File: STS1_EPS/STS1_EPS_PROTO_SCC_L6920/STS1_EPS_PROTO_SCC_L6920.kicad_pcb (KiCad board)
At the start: 2 copper layers, 15 parts, among them J1 Screw_Terminal_01x02, J2 Screw_Terminal_01x02, Q1 2N7000

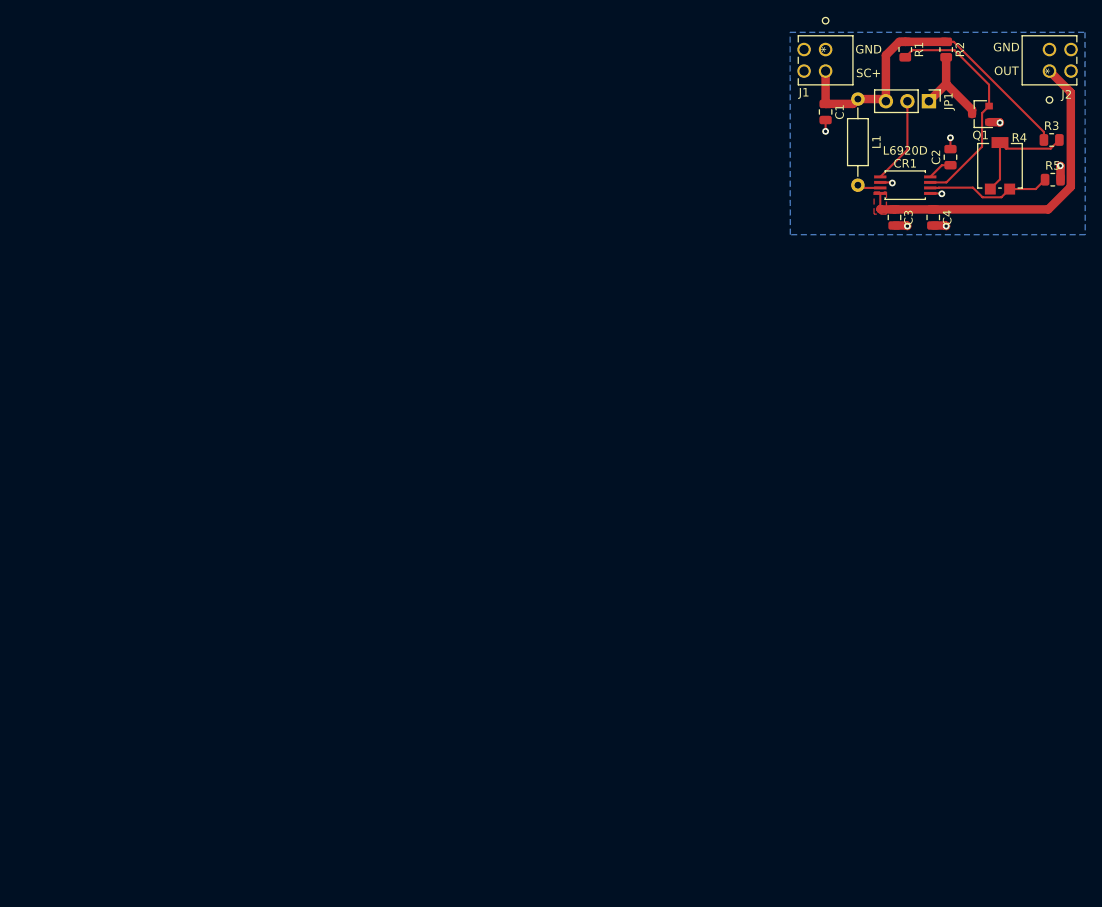
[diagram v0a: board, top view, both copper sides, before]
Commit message: - STS1_EPS_PROTO_SCC_L6920 now uses the STS1 PCB template and is again ready for review. - WOrked on STS1_EPS_PROTO_BCC_LTC4020.
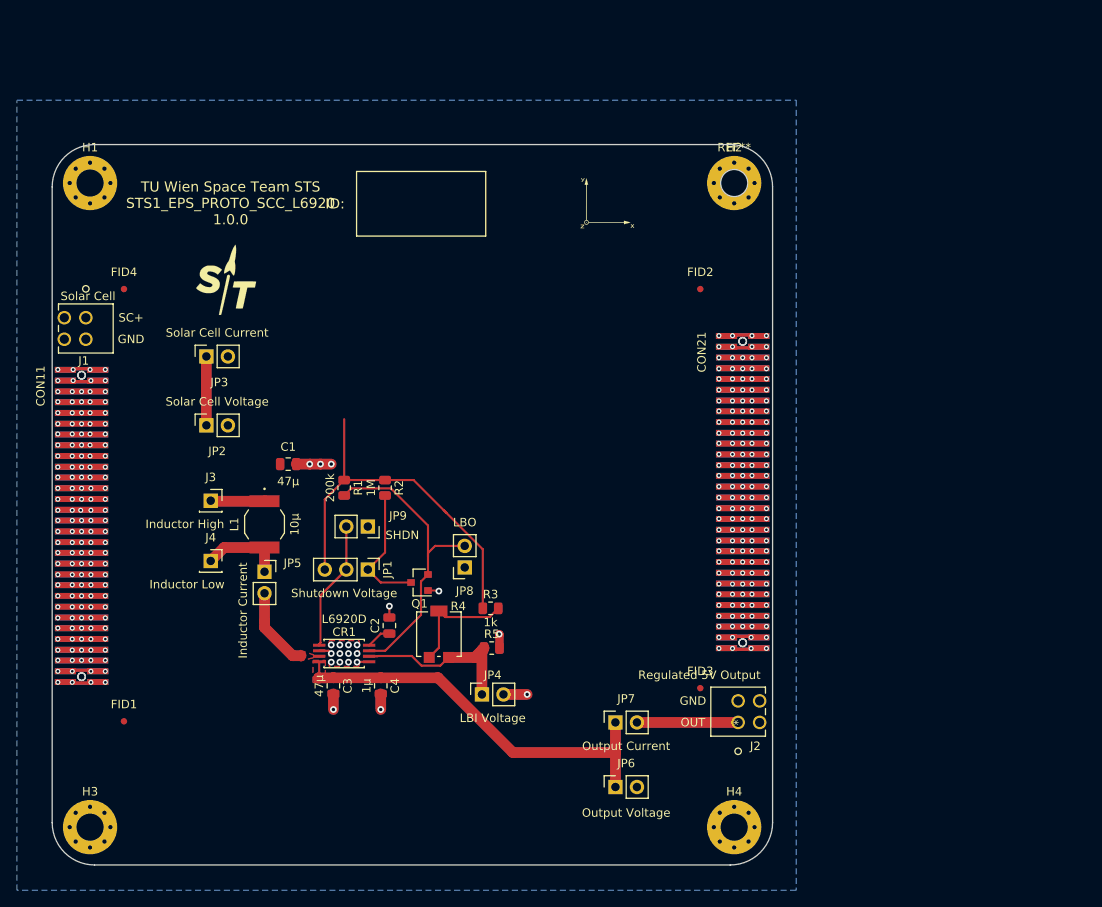
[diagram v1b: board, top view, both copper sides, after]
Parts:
- added CON1: DISCO-CON1, footprints:Cubesatconnector, B.Cu at (118.5, 85.9)
- added CON11: DISCO-CON1, footprints:Cubesatconnector, F.Cu at (118.5, 85.9)
- added CON2: DISCO-CON2, footprints:Cubesatconnector, B.Cu at (196.5, 81.9)
- added CON21: DISCO-CON2, footprints:Cubesatconnector, F.Cu at (196.5, 81.9)
- added FID1: Fiducial, Fiducial:Fiducial_0.75mm_Mask1.5mm, F.Cu at (123.5, 109.0)
- added FID2: Fiducial, Fiducial:Fiducial_0.75mm_Mask1.5mm, F.Cu at (191.5, 58.0)
- added FID3: Fiducial, Fiducial:Fiducial_0.75mm_Mask1.5mm, F.Cu at (191.5, 105.1)
- added FID4: Fiducial, Fiducial:Fiducial_0.75mm_Mask1.5mm, F.Cu at (123.5, 58.0)
- added G***: LOGO, spaceteam:STLogo, F.Cu at (135.6, 56.9)
- added H1: MountingHole_Pad, MountingHole:MountingHole_3.2mm_M3_Pad_Via, F.Cu at (119.5, 45.5)
- added H2: MountingHole_Pad, MountingHole:MountingHole_3.2mm_M3_Pad_Via, F.Cu at (195.5, 45.5)
- added H3: MountingHole_Pad, MountingHole:MountingHole_3.2mm_M3_Pad_Via, F.Cu at (119.5, 121.5)
- added H4: MountingHole_Pad, MountingHole:MountingHole_3.2mm_M3_Pad_Via, F.Cu at (195.5, 121.5)
- added J3: Inductor High, Connector_PinSocket_2.54mm:PinSocket_1x01_P2.54mm_Vertical, F.Cu at (133.7, 82.9)
- added J4: Inductor Low, Connector_PinSocket_2.54mm:PinSocket_1x01_P2.54mm_Vertical, F.Cu at (133.7, 90.1)
- added JP2: Solar Cell Voltage, Connector_PinSocket_2.54mm:PinSocket_1x02_P2.54mm_Vertical, F.Cu at (133.2, 74.1)
- added JP3: Solar Cell Current, Connector_PinSocket_2.54mm:PinSocket_1x02_P2.54mm_Vertical, F.Cu at (133.2, 65.9)
- added JP4: LBI Voltage, Connector_PinSocket_2.54mm:PinSocket_1x02_P2.54mm_Vertical, F.Cu at (165.7, 105.8)
- added JP5: Inductor Current, Connector_PinSocket_2.54mm:PinSocket_1x02_P2.54mm_Vertical, F.Cu at (140.0, 91.3)
- added JP6: Output Voltage, Connector_PinSocket_2.54mm:PinSocket_1x02_P2.54mm_Vertical, F.Cu at (181.4, 116.7)
- added JP7: Output Current, Connector_PinSocket_2.54mm:PinSocket_1x02_P2.54mm_Vertical, F.Cu at (181.4, 109.1)
- added JP8: LBO, Connector_PinSocket_2.54mm:PinSocket_1x02_P2.54mm_Vertical, F.Cu at (163.7, 90.8)
- added JP9: SHDN, Connector_PinSocket_2.54mm:PinSocket_1x02_P2.54mm_Vertical, F.Cu at (152.2, 86.0)
- added REF**: MountingHole_3.2mm_M3, Mounting_Holes:MountingHole_3.2mm_M3, F.Cu at (195.5, 45.5)
- added U1: coordinate_system, footprints:Coordinates, F.Cu at (180.5, 47.9)
- J1: value Screw_Terminal_01x02 -> Solar Cell
- J2: value Screw_Terminal_01x02 -> Regulated 5V Output
- JP1: value Jumper_NC_Dual -> Shutdown Voltage
- L1: value 1m -> 10µ; footprint Inductor_THT:L_Axial_L5.3mm_D2.2mm_P10.16mm_Horizontal_Vishay_IM-1 -> footprints:DO1608C-103C
- moved J1 92.8 mm to (119.0, 61.4)
- moved C2 86.2 mm to (154.8, 97.7)
- moved C3 86.2 mm to (148.2, 104.8)
- moved CR1 86.2 mm to (149.4, 101.0)
- moved R4 86.2 mm to (160.6, 98.7)
- moved R5 86.2 mm to (166.9, 100.3)
- moved JP1 86.2 mm to (152.2, 91.1)
- moved Q1 86.2 mm to (158.3, 92.6)
- moved R3 86.2 mm to (166.7, 95.6)
- moved L1 86.1 mm to (140.0, 85.7)
- moved C4 85.5 mm to (153.8, 104.8)
- moved J2 85.2 mm to (195.9, 109.1)
- moved R1 84.0 mm to (149.4, 81.4)
- moved R2 84.0 mm to (154.3, 81.4)
- moved C1 75.8 mm to (142.8, 78.6), turned to 0 degrees
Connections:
- C1 pad 1: /SC+ -> Net-(C1-Pad1)
- J1 pad 1: GND -> /SC+
- J1 pad 2: /SC+ -> GND
- J2 pad 1: Net-(C3-Pad1) -> Net-(J2-Pad1)
- L1 pad 1: /SC+ -> Net-(C1-Pad1)
- L1 pad 2: Net-(CR1-Pad7) -> Net-(J4-Pad1)
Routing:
- net /SC+: track 41.4 -> 54.3 mm
- net Net-(J2-Pad1): track 0.00 -> 11.9 mm
- net Net-(J4-Pad1): track 0.00 -> 9.87 mm
- net /LBO: track 27.6 -> 36.1 mm
- net Net-(C3-Pad1): track 40.3 -> 48.4 mm
- net Net-(CR1-Pad7): track 2.78 -> 9.74 mm
- net Net-(C1-Pad1): track 0.00 -> 6.47 mm
- net GND: track 11.6 -> 17.9 mm, vias 8 -> 56
- net /LBI: track 14.9 -> 20.5 mm
- net /*SHDN: track 10.3 -> 15.3 mm
- net Net-(JP1-Pad1): track 10.9 -> 15.3 mm
- net Net-(CON2-Pad9): vias 0 -> 5
- net Net-(CON2-Pad8): vias 0 -> 5
- net Net-(CON2-Pad7): vias 0 -> 5
- net Net-(CON2-Pad6): vias 0 -> 5
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- added copper zone on F.Cu, net GND
- added copper zone on F.Cu, net Net-(CR1-Pad7)
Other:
- board outline added: 85 x 85 mm
- net class Default: clearance 0.2 -> 0.1524; trace_width 0.25 -> 0.2032; via_dia 0.8 -> 0.6; via_drill 0.4 -> 0.3
- net class Supply added: clearance 0.1524, trace_width 0.508, via_dia 0.6, via_drill 0.3
- net class power removed
- rule pad_to_mask_clearance: 0 -> 0.19
- rule trace_clearance: 0.2 -> 0.1524
- board text added: "ID:"
- board text added: "TU Wien Space Team STS STS1_EPS_PROTO_SCC_L6920 1.0.0"

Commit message: Intermediate state.
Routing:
- net /SC+: track 54.3 -> 90.7 mm
- net Net-(C1-Pad1): track 6.47 -> 26.9 mm

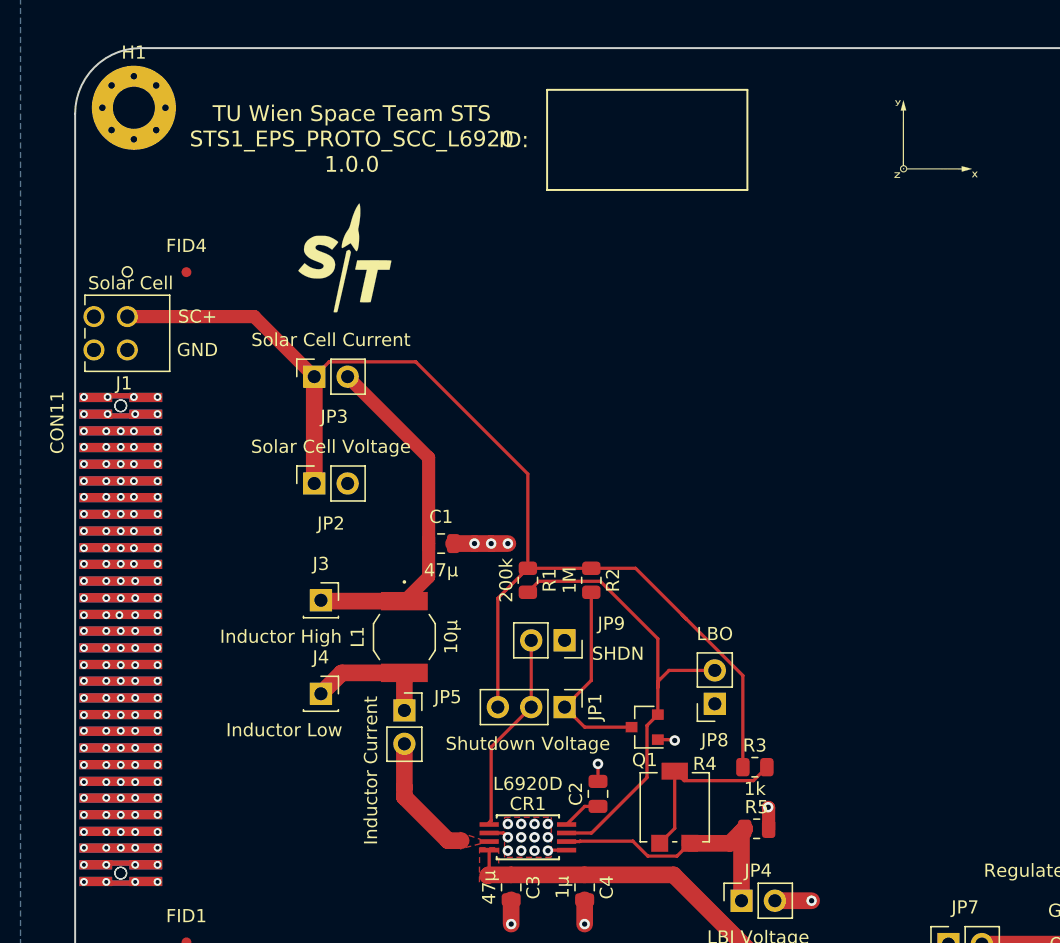
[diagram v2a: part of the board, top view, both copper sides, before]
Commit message: Incorporated feedback into BCC and SCC - Fixed "unspecified" pin type warnings - Added correct test point symbols - Added thermal blockers - Added DRC parameters and fixed DRC issues - Adapted CubeSat STS1 PCB template to not violate DRC
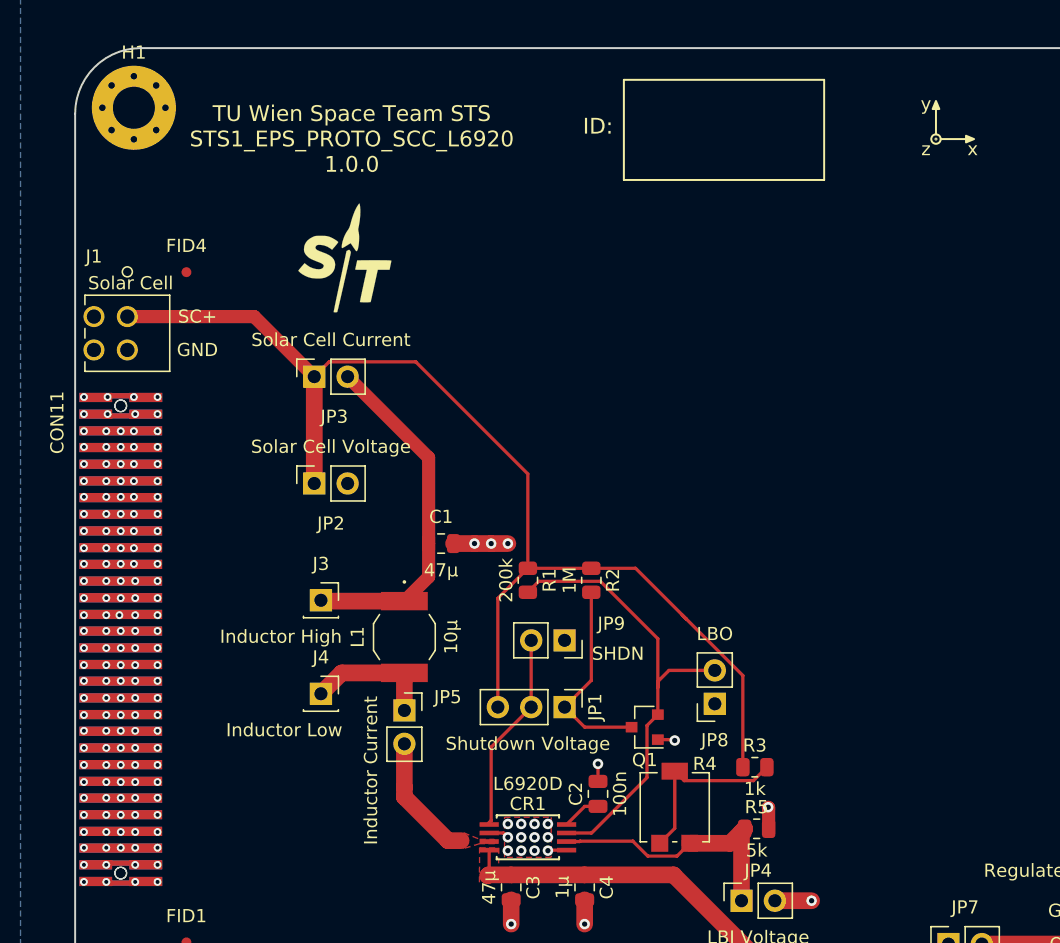
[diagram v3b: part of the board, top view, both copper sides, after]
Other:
- rule pad_to_mask_clearance: 0.19 -> 0
- rule trace_min: 0.2 -> 0.15
- rule via_min_size: 0.4 -> 0.3
